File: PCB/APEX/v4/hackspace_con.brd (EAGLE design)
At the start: 73.7 x 26.7 mm, 13 parts

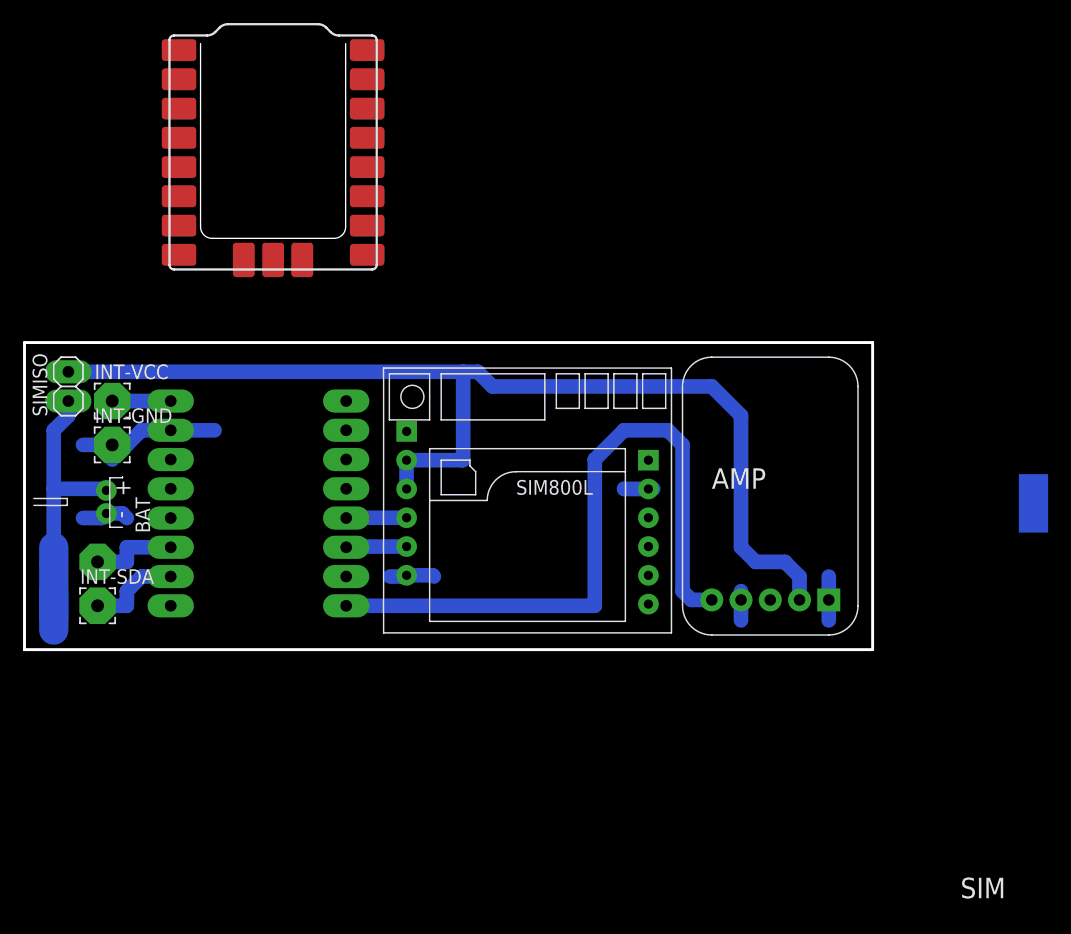
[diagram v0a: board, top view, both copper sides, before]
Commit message: ground pin 7
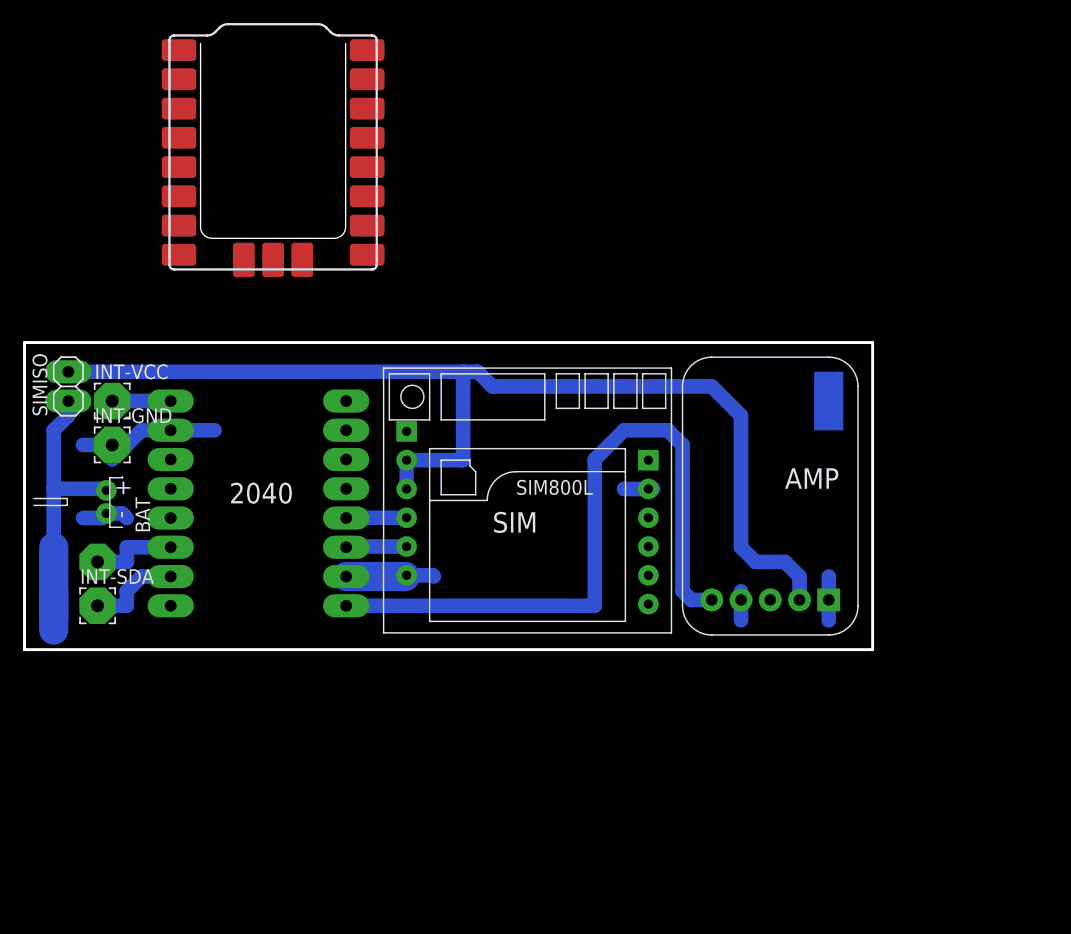
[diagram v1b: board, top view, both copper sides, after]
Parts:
- moved EXTGND 19.9 mm to (49.5, -35.6)
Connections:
- net GND: now also TINYLHS.7
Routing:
- net GND: track 30.2 -> 35.3 mm
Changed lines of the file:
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@@
 <dimension x1="-20.32" y1="-57.15" x2="53.34" y2="-57.15" x3="16.51" y3="-60.96" textsize="1.778" textratio="15" layer="49"/>
 <dimension x1="53.34" y1="-57.15" x2="53.34" y2="-30.48" x3="57.15" y3="-43.815" textsize="1.778" textratio="15" layer="49"/>
-<text x="60.96" y="-78.74" size="1.778" layer="21" font="vector" ratio="15">SIM</text>
-<text x="39.37" y="-43.18" size="1.778" layer="21" font="vector" ratio="15">AMP</text>
-<text x="71.12" y="-69.85" size="1.778" layer="22" font="vector" ratio="15" rot="MR0">2040</text>
+<text x="20.32" y="-46.99" size="1.778" layer="21" font="vector" ratio="15">SIM</text>
+<text x="45.72" y="-43.18" size="1.778" layer="21" font="vector" ratio="15">AMP</text>
+<text x="-2.54" y="-44.45" size="1.778" layer="21" font="vector" ratio="15">2040</text>
 </plain>
 <attributes>
@@
 <attribute name="VALUE" x="-17.78" y="-52.07" size="0.0254" layer="28" rot="MR180"/>
 </element>
-<element name="EXTGND" library="wirepad" library_urn="urn:adsk.eagle:library:412" package="SMD2,54-5,08" package3d_urn="urn:adsk.eagle:package:30841/1" value="" x="67.31" y="-44.45" smashed="yes" rot="MR0">
-<attribute name="NAME" x="68.81" y="-46.95" size="1.27" layer="26" rot="MR90"/>
-<attribute name="POPULARITY" value="21" x="67.31" y="-44.45" size="1.778" layer="28" font="vector" ratio="15" rot="MR0" display="off"/>
-<attribute name="VALUE" x="67.31" y="-44.45" size="0.0254" layer="28" rot="MR0"/>
+<element name="EXTGND" library="wirepad" library_urn="urn:adsk.eagle:library:412" package="SMD2,54-5,08" package3d_urn="urn:adsk.eagle:package:30841/1" value="" x="49.53" y="-35.56" smashed="yes" rot="MR0">
+<attribute name="NAME" x="51.03" y="-38.06" size="1.27" layer="26" rot="MR90"/>
+<attribute name="POPULARITY" value="21" x="49.53" y="-35.56" size="1.778" layer="28" font="vector" ratio="15" rot="MR0" display="off"/>
+<attribute name="VALUE" x="49.53" y="-35.56" size="0.0254" layer="28" rot="MR0"/>
 </element>
 <element name="BAT" library="adafruit" package="JST-PH-2-THM-RA" value="" x="-13.208" y="-44.323" smashed="yes" rot="R90">
@@
 <wire x1="33.868" y1="-43.196" x2="33.884" y2="-43.18" width="1.27" layer="16"/>
 <wire x1="33.884" y1="-43.18" x2="34.29" y2="-43.18" width="1.27" layer="16"/>
+<contactref element="TINYLHS" pad="7"/>
+<wire x1="7.62" y1="-50.8" x2="12.764" y2="-50.8" width="2.54" layer="16"/>
 <wire x1="1.27" y1="-23.3" x2="-6.9" y2="-22.86" width="0" layer="19" extent="1-1"/>
 <wire x1="-6.9" y1="-7.62" x2="-6.9" y2="-22.86" width="0" layer="19" extent="1-1"/>
 <wire x1="-7.62" y1="-38.1" x2="-6.9" y2="-22.86" width="0" layer="19" extent="1-1"/>
-<wire x1="67.31" y1="-44.45" x2="49.53" y2="-50.8" width="0" layer="19" extent="16-16"/>
+<wire x1="49.53" y1="-35.56" x2="49.53" y2="-50.8" width="0" layer="19" extent="16-16"/>
 </signal>
 <signal name="VCC">
@@
 <contactref element="U$1" pad="RX"/>
 <wire x1="8.914" y1="-45.696" x2="8.89" y2="-45.72" width="1.524" layer="1"/>
-<wire x1="7.62" y1="-45.72" x2="7.644" y2="-45.696" width="1.27" layer="16"/>
-<wire x1="7.644" y1="-45.696" x2="12.868" y2="-45.696" width="1.27" layer="16"/>
+<wire x1="7.644" y1="-45.696" x2="7.62" y2="-45.72" width="1.27" layer="16"/>
+<wire x1="12.868" y1="-45.696" x2="7.644" y2="-45.696" width="1.27" layer="16"/>
 <wire x1="7.62" y1="-45.72" x2="8.89" y2="-45.72" width="0" layer="19" extent="1-1"/>
 <wire x1="9.44" y1="-15.24" x2="8.914" y2="-45.696" width="0" layer="19" extent="1-1"/>

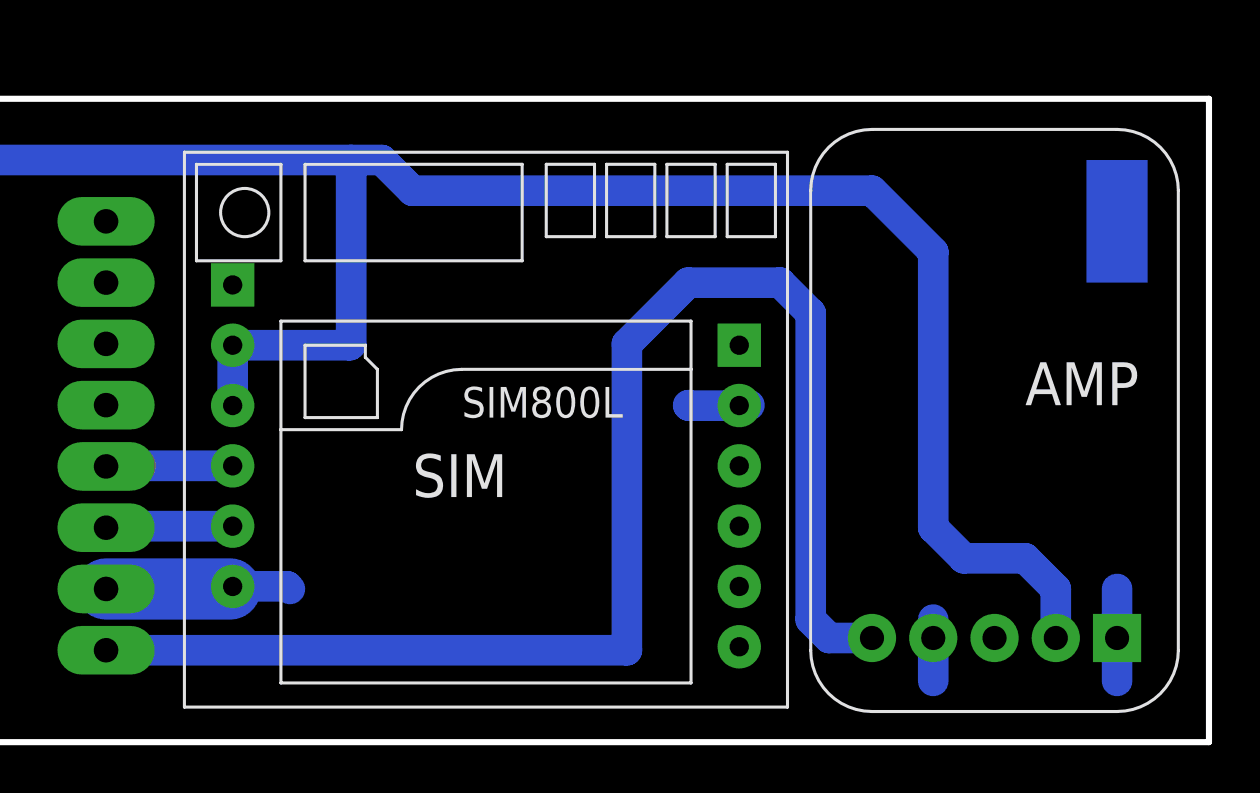
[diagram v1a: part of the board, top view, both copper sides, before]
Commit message: embiggen pads
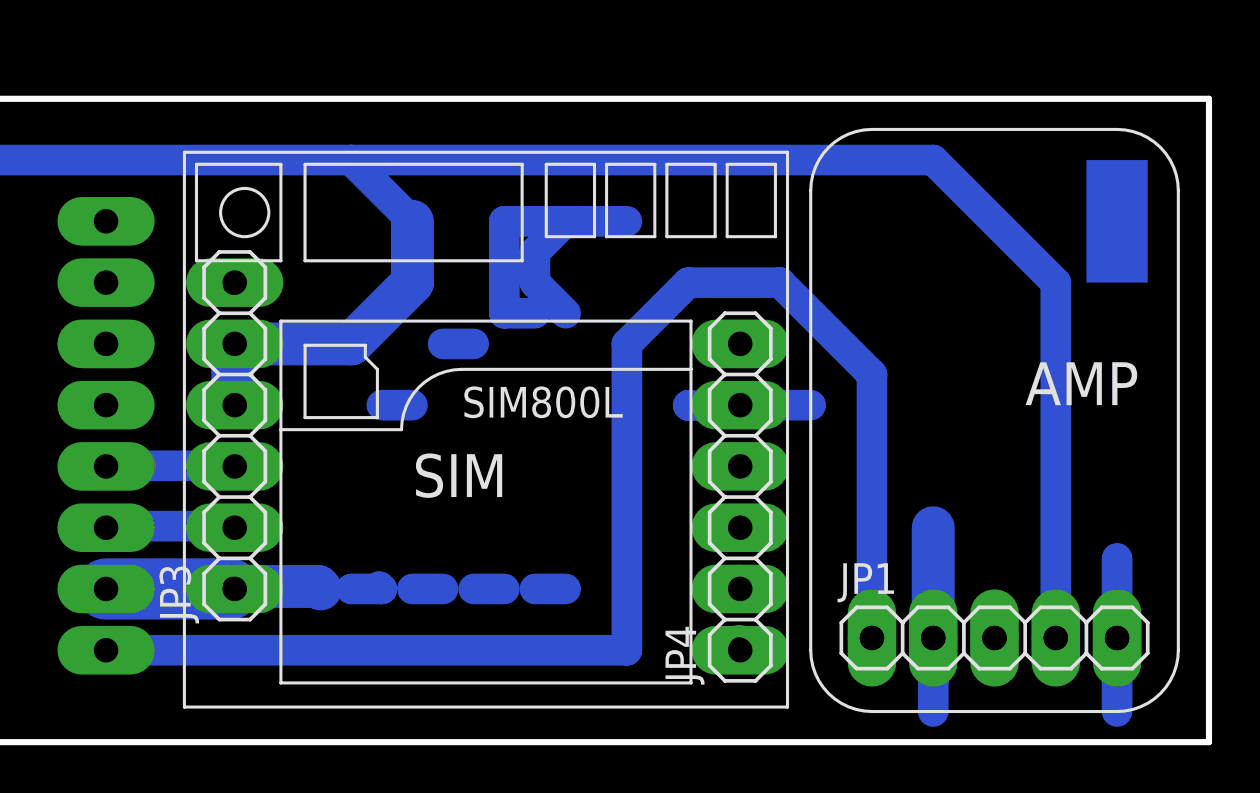
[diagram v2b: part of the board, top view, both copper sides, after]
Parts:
- added JP1: (no value), pinhead:1X05
- added JP3, JP4: (no value), pinhead:1X06
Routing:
- net GND: track 35.3 -> 71.3 mm
- net SIMPOW: track 94.6 -> 102.4 mm
- net AIN+: track 59.0 -> 58.0 mm
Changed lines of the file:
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@@
 <attribute name="VALUE" x="50.8" y="-50.927" size="0.4064" layer="27" ratio="10" rot="R180"/>
+</element>
+<element name="JP1" library="pinhead" library_urn="urn:adsk.eagle:library:325" package="1X05" package3d_urn="urn:adsk.eagle:package:22469/2" value="" x="44.45" y="-52.832" smashed="yes">
+<attribute name="NAME" x="38.0238" y="-51.0032" size="1.27" layer="25" ratio="10"/>
+<attribute name="POPULARITY" value="69" x="44.45" y="-52.832" size="1.778" layer="27" font="vector" ratio="15" display="off"/>
+<attribute name="VALUE" x="38.1" y="-56.007" size="1.27" layer="27"/>
+</element>
+<element name="JP3" library="pinhead" library_urn="urn:adsk.eagle:library:325" package="1X06" package3d_urn="urn:adsk.eagle:package:22472/2" value="" x="12.954" y="-44.45" smashed="yes" rot="R90">
+<attribute name="NAME" x="11.1252" y="-52.1462" size="1.27" layer="25" ratio="10" rot="R90"/>
+<attribute name="POPULARITY" value="79" x="12.954" y="-44.45" size="1.778" layer="27" font="vector" ratio="15" rot="R90" display="off"/>
+<attribute name="VALUE" x="16.129" y="-52.07" size="1.27" layer="27" rot="R90"/>
+</element>
+<element name="JP4" library="pinhead" library_urn="urn:adsk.eagle:library:325" package="1X06" package3d_urn="urn:adsk.eagle:package:22472/2" value="" x="33.909" y="-46.99" smashed="yes" rot="R90">
+<attribute name="NAME" x="32.0802" y="-54.6862" size="1.27" layer="25" ratio="10" rot="R90"/>
+<attribute name="POPULARITY" value="79" x="33.909" y="-46.99" size="1.778" layer="27" font="vector" ratio="15" rot="R90" display="off"/>
+<attribute name="VALUE" x="37.084" y="-54.61" size="1.27" layer="27" rot="R90"/>
 </element>
 </elements>
@@
 </polygon>
 <wire x1="-11.43" y1="-39.37" x2="-10.16" y2="-38.1" width="1.27" layer="16"/>
-<wire x1="41.91" y1="-52.07" x2="41.91" y2="-52.832" width="1.27" layer="16"/>
+<wire x1="41.91" y1="-52.832" x2="41.91" y2="-52.07" width="1.27" layer="16"/>
 <wire x1="41.91" y1="-52.832" x2="41.91" y2="-54.61" width="1.27" layer="16"/>
-<wire x1="49.53" y1="-50.8" x2="49.53" y2="-52.832" width="1.27" layer="16"/>
-<wire x1="49.53" y1="-52.832" x2="49.53" y2="-54.61" width="1.27" layer="16"/>
-<wire x1="12.868" y1="-50.696" x2="15.136" y2="-50.696" width="1.27" layer="16"/>
-<wire x1="15.136" y1="-50.696" x2="15.24" y2="-50.8" width="1.27" layer="16"/>
 <wire x1="12.868" y1="-50.696" x2="12.764" y2="-50.8" width="1.27" layer="16"/>
 <wire x1="12.764" y1="-50.8" x2="11.43" y2="-50.8" width="1.27" layer="16"/>
@@
 <wire x1="33.868" y1="-43.196" x2="31.766" y2="-43.196" width="1.27" layer="16"/>
 <wire x1="31.766" y1="-43.196" x2="31.75" y2="-43.18" width="1.27" layer="16"/>
-<wire x1="33.868" y1="-43.196" x2="33.884" y2="-43.18" width="1.27" layer="16"/>
-<wire x1="33.884" y1="-43.18" x2="34.29" y2="-43.18" width="1.27" layer="16"/>
 <contactref element="TINYLHS" pad="7"/>
 <wire x1="7.62" y1="-50.8" x2="12.764" y2="-50.8" width="2.54" layer="16"/>
+<wire x1="33.868" y1="-43.196" x2="33.884" y2="-43.18" width="1.27" layer="16"/>
+<wire x1="33.884" y1="-43.18" x2="36.83" y2="-43.18" width="1.27" layer="16"/>
+<wire x1="41.91" y1="-52.832" x2="41.91" y2="-55.88" width="1.27" layer="16"/>
+<wire x1="49.53" y1="-52.832" x2="49.53" y2="-55.88" width="1.27" layer="16"/>
+<wire x1="49.53" y1="-52.832" x2="49.53" y2="-49.53" width="1.27" layer="16"/>
+<wire x1="25.4" y1="-36.83" x2="25.4" y2="-38.1" width="1.27" layer="16"/>
+<wire x1="25.4" y1="-36.83" x2="26.67" y2="-35.56" width="1.27" layer="16"/>
+<wire x1="26.67" y1="-35.56" x2="29.21" y2="-35.56" width="1.27" layer="16"/>
+<wire x1="25.4" y1="-38.1" x2="26.67" y2="-39.37" width="1.27" layer="16"/>
+<wire x1="26.67" y1="-50.8" x2="25.4" y2="-50.8" width="1.27" layer="16"/>
+<wire x1="25.4" y1="-39.37" x2="24.13" y2="-39.37" width="1.27" layer="16"/>
+<wire x1="24.13" y1="-50.8" x2="22.86" y2="-50.8" width="1.27" layer="16"/>
+<wire x1="22.86" y1="-40.64" x2="21.59" y2="-40.64" width="1.27" layer="16"/>
+<wire x1="21.59" y1="-50.8" x2="20.32" y2="-50.8" width="1.27" layer="16"/>
+<wire x1="20.32" y1="-43.18" x2="19.05" y2="-43.18" width="1.27" layer="16"/>
+<wire x1="17.78" y1="-50.8" x2="19.05" y2="-50.8" width="1.27" layer="16"/>
+<wire x1="18.946" y1="-50.696" x2="19.05" y2="-50.8" width="1.27" layer="16"/>
+<wire x1="24.13" y1="-39.37" x2="24.13" y2="-35.56" width="1.27" layer="16"/>
+<wire x1="24.13" y1="-35.56" x2="26.67" y2="-35.56" width="1.27" layer="16"/>
+<wire x1="12.868" y1="-50.696" x2="16.406" y2="-50.696" width="1.778" layer="16"/>
+<wire x1="16.406" y1="-50.696" x2="16.51" y2="-50.8" width="1.778" layer="16"/>
+<wire x1="41.91" y1="-52.07" x2="41.91" y2="-48.26" width="1.778" layer="16"/>
 <wire x1="1.27" y1="-23.3" x2="-6.9" y2="-22.86" width="0" layer="19" extent="1-1"/>
 <wire x1="-6.9" y1="-7.62" x2="-6.9" y2="-22.86" width="0" layer="19" extent="1-1"/>
 <wire x1="-7.62" y1="-38.1" x2="-6.9" y2="-22.86" width="0" layer="19" extent="1-1"/>
-<wire x1="49.53" y1="-35.56" x2="49.53" y2="-50.8" width="0" layer="19" extent="16-16"/>
 </signal>
 <signal name="VCC">
@@
 <contactref element="U$1" pad="RST"/>
 <contactref element="JP2" pad="2"/>
-<wire x1="17.78" y1="-33.02" x2="17.78" y2="-40.64" width="1.27" layer="16"/>
 <wire x1="17.78" y1="-40.64" x2="17.724" y2="-40.696" width="1.27" layer="16"/>
 <wire x1="17.724" y1="-40.696" x2="12.868" y2="-40.696" width="1.27" layer="16"/>
-<wire x1="12.868" y1="-40.696" x2="12.868" y2="-43.196" width="1.27" layer="16"/>
 <wire x1="-16.51" y1="-33.02" x2="17.78" y2="-33.02" width="1.27" layer="16"/>
-<wire x1="17.78" y1="-33.02" x2="19.05" y2="-33.02" width="1.27" layer="16"/>
-<wire x1="46.99" y1="-52.832" x2="46.99" y2="-50.8" width="1.27" layer="16"/>
-<wire x1="46.99" y1="-50.8" x2="45.72" y2="-49.53" width="1.27" layer="16"/>
-<wire x1="45.72" y1="-49.53" x2="43.18" y2="-49.53" width="1.27" layer="16"/>
-<wire x1="43.18" y1="-49.53" x2="41.91" y2="-48.26" width="1.27" layer="16"/>
-<wire x1="41.91" y1="-48.26" x2="41.91" y2="-36.83" width="1.27" layer="16"/>
-<wire x1="41.91" y1="-36.83" x2="39.37" y2="-34.29" width="1.27" layer="16"/>
-<wire x1="20.32" y1="-34.29" x2="19.05" y2="-33.02" width="1.27" layer="16"/>
-<wire x1="39.37" y1="-34.29" x2="20.32" y2="-34.29" width="1.27" layer="16"/>
+<wire x1="20.32" y1="-35.56" x2="17.78" y2="-33.02" width="1.27" layer="16"/>
+<wire x1="12.868" y1="-40.696" x2="12.868" y2="-43.196" width="1.778" layer="16"/>
+<wire x1="12.868" y1="-40.696" x2="12.924" y2="-40.64" width="1.778" layer="16"/>
+<wire x1="12.924" y1="-40.64" x2="17.78" y2="-40.64" width="1.778" layer="16"/>
+<wire x1="17.78" y1="-40.64" x2="20.32" y2="-38.1" width="1.778" layer="16"/>
+<wire x1="20.32" y1="-38.1" x2="20.32" y2="-35.56" width="1.778" layer="16"/>
+<wire x1="17.78" y1="-33.02" x2="41.91" y2="-33.02" width="1.27" layer="16"/>
+<wire x1="46.99" y1="-38.1" x2="41.91" y2="-33.02" width="1.27" layer="16"/>
+<wire x1="46.99" y1="-52.832" x2="46.99" y2="-38.1" width="1.27" layer="16"/>
 </signal>
 <signal name="AIN+">
@@
 <contactref element="A1" pad="7"/>
 <contactref element="TINYLHS" pad="8"/>
-<wire x1="37.592" y1="-52.832" x2="36.83" y2="-52.07" width="1.27" layer="16"/>
-<wire x1="37.592" y1="-52.832" x2="39.37" y2="-52.832" width="1.27" layer="16"/>
-<wire x1="36.83" y1="-52.07" x2="36.83" y2="-39.37" width="1.27" layer="16"/>
-<wire x1="36.83" y1="-39.37" x2="35.56" y2="-38.1" width="1.27" layer="16"/>
+<wire x1="39.37" y1="-52.832" x2="39.37" y2="-41.91" width="1.27" layer="16"/>
+<wire x1="39.37" y1="-41.91" x2="35.56" y2="-38.1" width="1.27" layer="16"/>
 <wire x1="31.75" y1="-38.1" x2="29.21" y2="-40.64" width="1.27" layer="16"/>
 <wire x1="29.21" y1="-40.64" x2="29.21" y2="-53.34" width="1.27" layer="16"/>
